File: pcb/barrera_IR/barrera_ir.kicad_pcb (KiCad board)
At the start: 2 copper layers, 16 parts, among them J1 RJ45, P1 DIN_5, P2 DIN_5, U1 LM358N

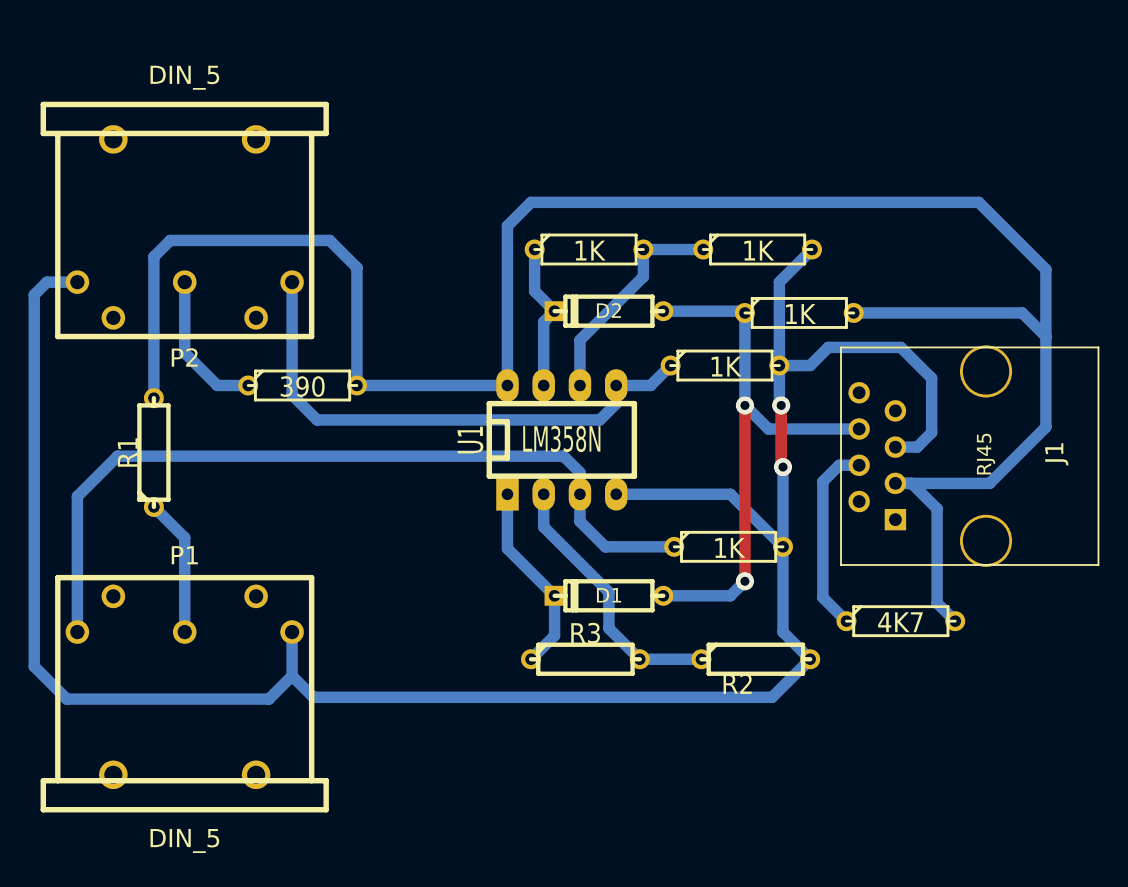
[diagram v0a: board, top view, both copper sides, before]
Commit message: correction bug in circuit of infra red barrier
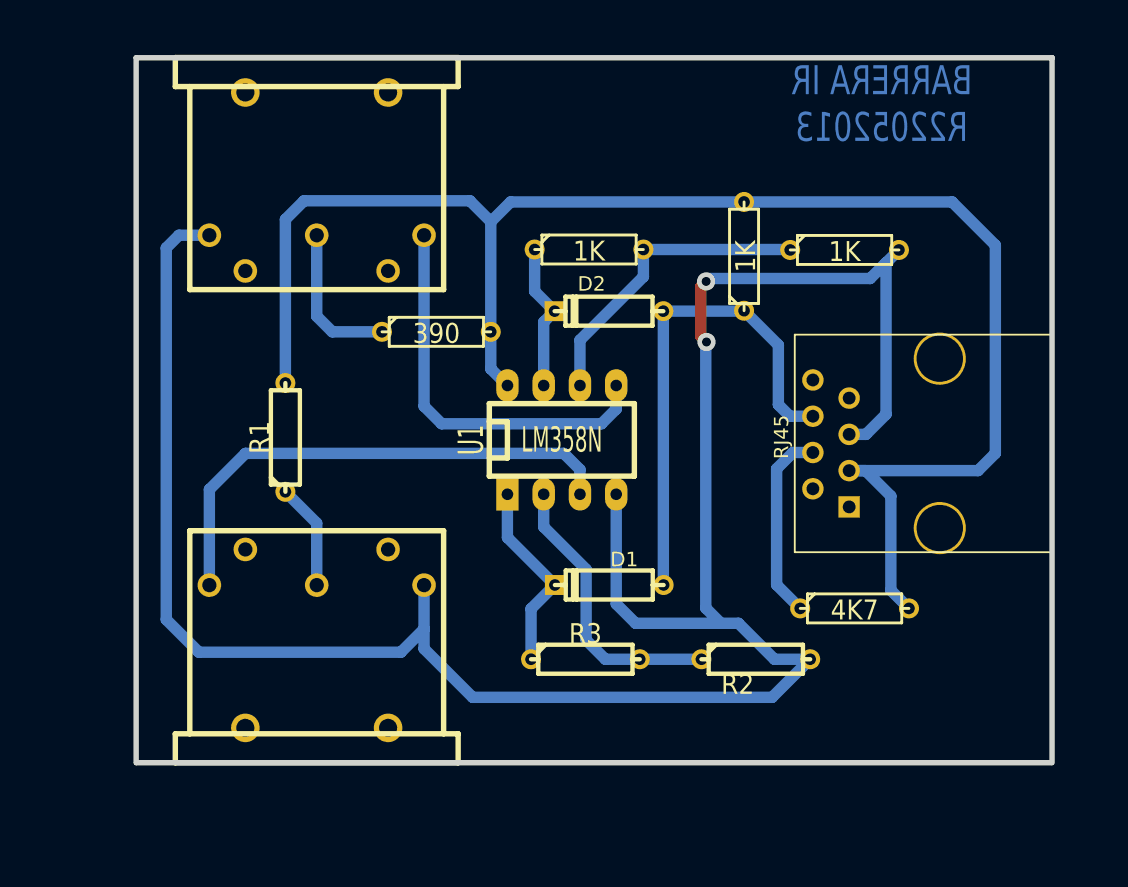
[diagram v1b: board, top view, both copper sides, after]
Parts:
- removed R10, R9: 1K, R3
- moved R4 10.1 mm to (111.6, 71.2)
- moved P1 9.81 mm to (103.2, 88.9)
- moved P2 9.81 mm to (103.2, 64.4)
- moved R1 9.27 mm to (101.0, 78.6)
- moved R5 6.09 mm to (140.2, 65.4)
- moved R7 5.54 mm to (133.2, 65.9), turned to 90 degrees
- moved J1 3.36 mm to (146.9, 79.0)
- moved R8 3.36 mm to (140.9, 90.5)
- moved D1 0.76 mm to (123.7, 88.9)
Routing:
- net Vcc: track 145.1 -> 113.5 mm
- net N-0000012: track 57.1 -> 35.9 mm
- net N-0000013: track 37.5 -> 28.0 mm
- net GND: track 152.8 -> 158.9 mm
- net N-000002: track 15.6 -> 21.7 mm
- net AN: track 39.4 -> 35.2 mm, vias 2 -> 0
- net N-000001: track 9.66 -> 7.45 mm
- net N-000005: track 18.7 -> 20.1 mm
- added copper zone on B.Cu, net GND
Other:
- board outline added: 64.2 x 49.4 mm
- board text added: "BARRERA IR R22052013"

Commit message: Change the wired AND for wired OR in the output of barrier IR
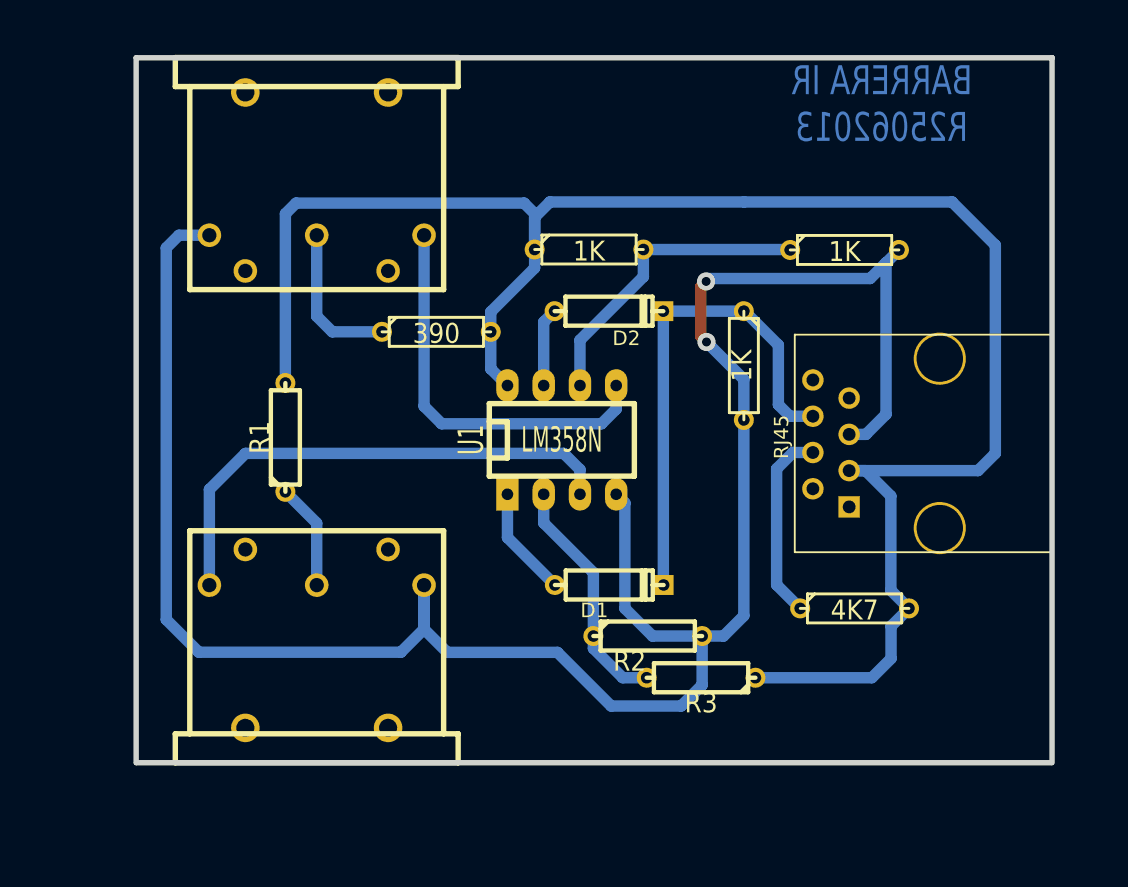
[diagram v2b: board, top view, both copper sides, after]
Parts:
- moved R3 8.21 mm to (130.1, 95.4), turned to 180 degrees
- moved R2 7.74 mm to (126.4, 92.5)
- moved R7 7.65 mm to (133.1, 73.5), turned to 270 degrees
- turned D1 to 0 degrees
- turned D2 to 0 degrees
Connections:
- D1 pad 1: AN -> N-000004
- D1 pad 2: N-000004 -> AN
- D2 pad 1: AN -> N-000001
- D2 pad 2: N-0000017 -> AN
- R3 pad 1: N-000004 -> Vcc
- R6 pad 1: N-0000017 -> Vcc
- R7 pad 2: Vcc -> GND
- U1 pad 7: N-0000017 -> N-000001
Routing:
- net Vcc: track 113.5 -> 131.4 mm
- net N-0000017: track 10.4 -> 0.00 mm
- net GND: track 158.9 -> 152.1 mm
- net N-000004: track 13.6 -> 7.73 mm
- net N-000001: track 0.00 -> 5.52 mm
- net N-000005: track 20.1 -> 16.8 mm
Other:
- board text added: "BARRERA IR R25062013"
- board text removed: "BARRERA IR R22052013"
